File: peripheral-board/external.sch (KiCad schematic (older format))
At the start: 0 parts

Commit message: keyboard switches and diodes placed
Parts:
- added CONN8001: 10056847-XY1LF, lib:10056847-XY1LF, symbol 10056847-XY1LF
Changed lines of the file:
@@
 $Descr A4 11693 8268
 encoding utf-8
-Sheet 1 9
+Sheet 8 9
 Title ""
 Date ""
@@
 Comment4 ""
 $EndDescr
+$Comp
+L 10056847-XY1LF CONN8001
+U 1 1 581F82EF
+P 5550 2150
+F 0 "CONN8001" H 5550 2937 60  0000 C CNN
+F 1 "10056847-XY1LF" H 5550 2831 60  0000 C CNN
+F 2 "lib:10056847-XY1LF" H 5550 2150 60  0001 C CNN
+F 3 "" H 5550 2150 60  0001 C CNN
+	1    5550 2150
+	1    0    0    -1
+$EndComp
 $EndSCHEMATC

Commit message: lol
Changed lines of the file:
@@
 	1    0    0    -1
 $EndComp
+Text HLabel 2300 1650 0    60   Output ~ 0
+MISO
+Text HLabel 2300 1750 0    60   Input ~ 0
+MOSI
+Text HLabel 2300 1850 0    60   Input ~ 0
+SCK
+Text HLabel 2300 2050 0    60   Input ~ 0
+SS1
+Text HLabel 2300 2150 0    60   Input ~ 0
+SS2
+Text HLabel 2300 2250 0    60   Input ~ 0
+SS3
+Text HLabel 2300 2350 0    60   Input ~ 0
+SS4
+Text HLabel 2300 2550 0    60   Output ~ 0
+INTERRUPT
+Text HLabel 2300 2800 0    60   Input ~ 0
+TX
+Text HLabel 2300 2900 0    60   Output ~ 0
+RX
+Text HLabel 2300 3150 0    60   BiDi ~ 0
+SDA
+Text HLabel 2300 3250 0    60   Input ~ 0
+SCL
+Text HLabel 2300 3550 0    60   Output ~ 0
+DETECT1
+Text HLabel 2300 3650 0    60   Output ~ 0
+DETECT2
+Text HLabel 2300 3750 0    60   Output ~ 0
+DETECT3
+Text HLabel 2300 3850 0    60   Output ~ 0
+DETECT4
 $EndSCHEMATC

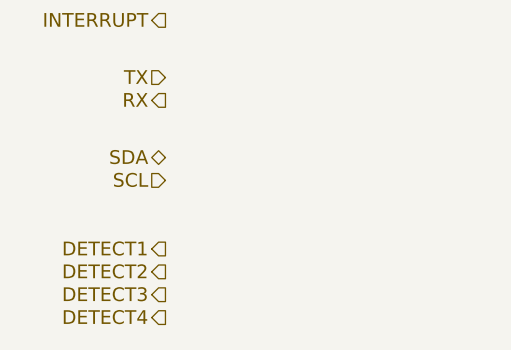
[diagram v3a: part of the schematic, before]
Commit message: some more keyboard stuff fit on this side..
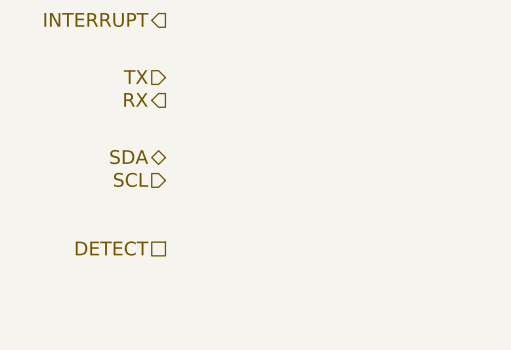
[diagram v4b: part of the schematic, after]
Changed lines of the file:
@@
 Text HLabel 2300 3250 0    60   Input ~ 0
 SCL
-Text HLabel 2300 3550 0    60   Output ~ 0
-DETECT1
-Text HLabel 2300 3650 0    60   Output ~ 0
-DETECT2
-Text HLabel 2300 3750 0    60   Output ~ 0
-DETECT3
-Text HLabel 2300 3850 0    60   Output ~ 0
-DETECT4
+Text HLabel 2300 3550 0    60   UnSpc ~ 0
+DETECT
 $EndSCHEMATC

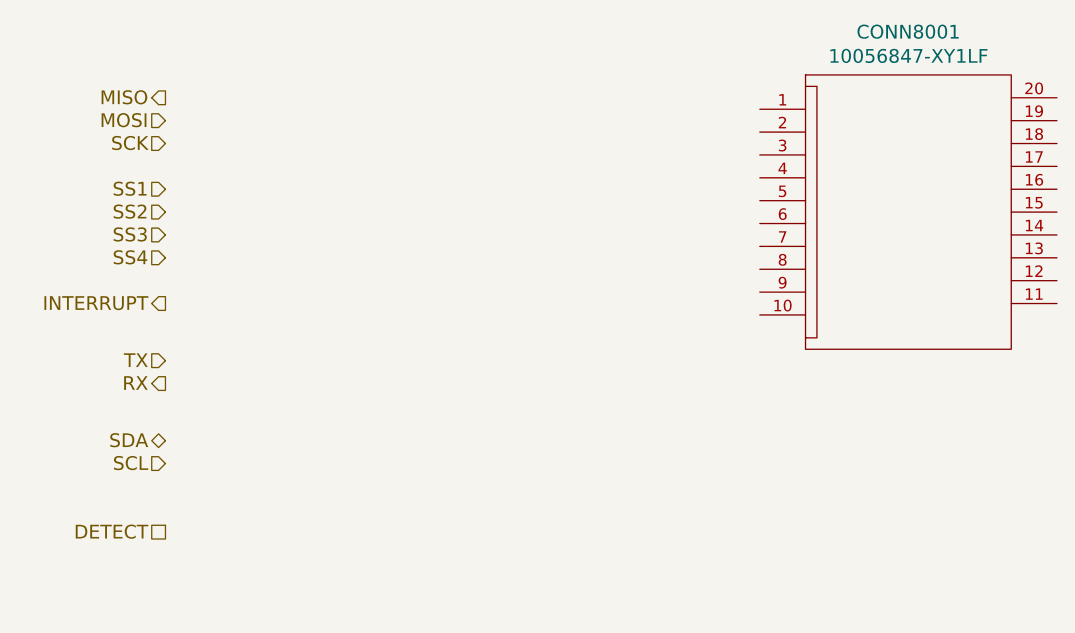
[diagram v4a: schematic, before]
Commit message: added some audio circuitry
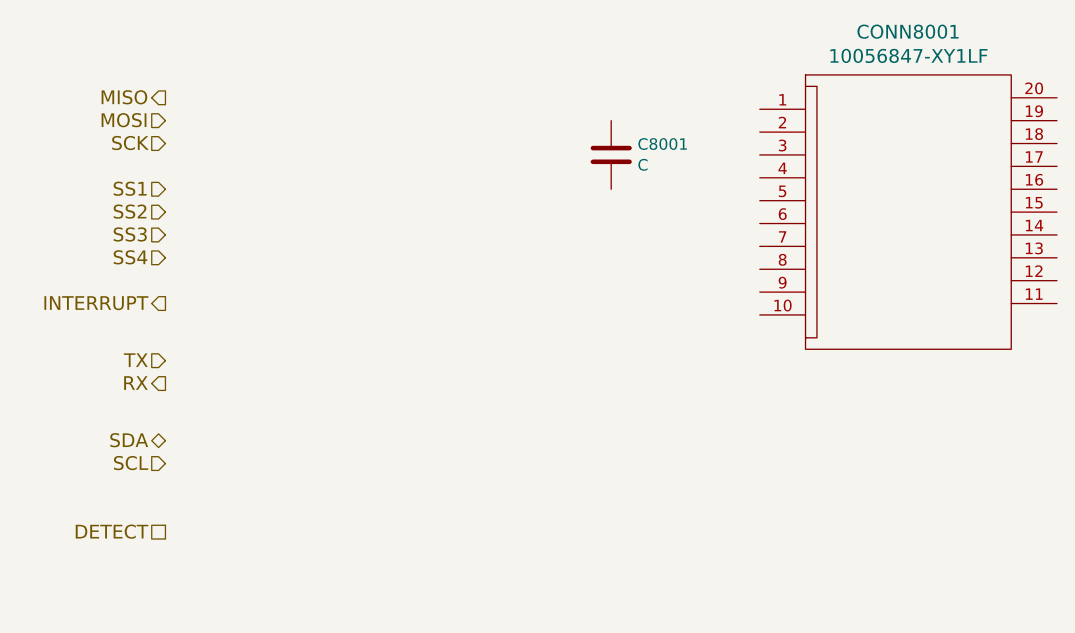
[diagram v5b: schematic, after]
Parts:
- added C8001: C, symbol C
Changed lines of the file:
@@
 LIBS:switchmode
 LIBS:joystick
+LIBS:digital-pot
 LIBS:peripheral-board-cache
-EELAYER 25 0
+EELAYER 26 0
 EELAYER END
 $Descr A4 11693 8268
@@
 Text HLabel 2300 3550 0    60   UnSpc ~ 0
 DETECT
+$Comp
+L C C8001
+U 1 1 58246CCC
+P 4250 1900
+F 0 "C8001" H 4365 1946 50  0000 L CNN
+F 1 "C" H 4365 1855 50  0000 L CNN
+F 2 "" H 4288 1750 50  0000 C CNN
+F 3 "" H 4250 1900 50  0000 C CNN
+	1    4250 1900
+	1    0    0    -1
+$EndComp
 $EndSCHEMATC

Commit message: audio circuitry
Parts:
- renumbered C8001 to C9001, CONN8001 to CONN9001
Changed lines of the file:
@@
 EESchema Schematic File Version 2
+LIBS:peripheral-board-rescue
 LIBS:power
 LIBS:device
@@
 LIBS:digital-pot
 LIBS:vref
+LIBS:switches
 LIBS:peripheral-board-cache
 EELAYER 26 0
@@
 $EndDescr
 $Comp
-L 10056847-XY1LF CONN8001
+L 10056847-XY1LF CONN9001
 U 1 1 581F82EF
 P 5550 2150
-F 0 "CONN8001" H 5550 2937 60  0000 C CNN
+F 0 "CONN9001" H 5550 2937 60  0000 C CNN
 F 1 "10056847-XY1LF" H 5550 2831 60  0000 C CNN
 F 2 "lib:10056847-XY1LF" H 5550 2150 60  0001 C CNN
@@
 DETECT
 $Comp
-L C C8001
+L C C9001
 U 1 1 58246CCC
 P 4250 1900
-F 0 "C8001" H 4365 1946 50  0000 L CNN
+F 0 "C9001" H 4365 1946 50  0000 L CNN
 F 1 "C" H 4365 1855 50  0000 L CNN
 F 2 "" H 4288 1750 50  0001 C CNN
